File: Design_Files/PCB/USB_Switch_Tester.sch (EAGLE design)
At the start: 7 parts, among them SW1 STX-3120

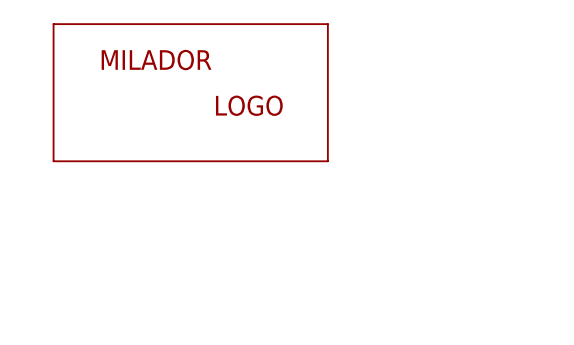
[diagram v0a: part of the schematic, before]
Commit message: Updated PCB: Added MMC Logo
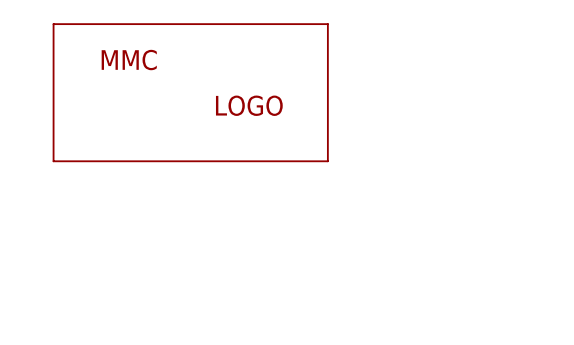
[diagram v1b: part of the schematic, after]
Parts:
- LABEL_LOGO: value MILADOR-LOGO-SM -> MMC_LOGO-XSM; device milador:MILADOR-LOGO-SM -> MMC Eagle:MMC_LOGO-XSM
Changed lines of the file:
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@@
 <part name="U$3" library="supply1" library_urn="urn:adsk.eagle:library:371" deviceset="GND" device=""/>
 <part name="SJ1" library="MMC_SMD" library_urn="urn:adsk.eagle:library:30840833" deviceset="SOLDERJUMPER" device="REFLOW" package3d_urn="urn:adsk.eagle:package:30840956/1"/>
-<part name="LABEL_LOGO" library="milador" library_urn="urn:adsk.eagle:library:12595918" deviceset="MILADOR-LOGO-" device="SM" package3d_urn="urn:adsk.eagle:package:36266468/1"/>
+<part name="LABEL_LOGO" library="MMC Eagle" library_urn="urn:adsk.eagle:library:13126479" deviceset="MMC_LOGO-" device="XSM" package3d_urn="urn:adsk.eagle:package:36433256/2" value="MMC_LOGO-XSM"/>
 </parts>
 <sheets>
